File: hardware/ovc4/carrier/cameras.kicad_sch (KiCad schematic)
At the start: 7 parts, among them U1 Jetson_Nano, U12 PICAM, U13 PICAM, U14 PICAM, U15 PICAM, U16 PICAM, U17 PICAM

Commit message: Finished first iteration of placement and routing
Signed-off-by: Luca Della Vedova <luca@openrobotics.org>
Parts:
- added J7: Conn_01x05, Connector_PinHeader_2.54mm:PinHeader_1x05_P2.54mm_Vertical, symbol Connector_Generic:Conn_01x05
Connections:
- net CAM1_ENABLE: now also J7.3 (Pin_3)
- net CAM1_SCL_1V8: now also J7.4 (Pin_4)
- net CAM1_SDA_1V8: now also J7.5 (Pin_5)
- net CAM1_TRIGGER: now also J7.2 (Pin_2)
- net GND: now also J7.1 (Pin_1)
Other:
- note added: "For debugging"
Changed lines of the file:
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@@
   (junction (at 226.06 124.46))
   (junction (at 226.06 132.08))
+  (no_connect (at 39.37 128.27))
+  (no_connect (at 39.37 153.67))
+  (no_connect (at 39.37 138.43))
+  (no_connect (at 39.37 140.97))
+  (no_connect (at 39.37 125.73))
   (no_connect (at 39.37 130.81))
-  (no_connect (at 39.37 138.43))
+  (no_connect (at 39.37 156.21))
   (no_connect (at 39.37 133.35))
-  (no_connect (at 39.37 156.21))
   (no_connect (at 39.37 146.05))
-  (no_connect (at 39.37 153.67))
-  (no_connect (at 39.37 125.73))
-  (no_connect (at 39.37 128.27))
-  (no_connect (at 39.37 140.97))
   (no_connect (at 39.37 148.59))
   (wire (pts (xy 116.84 50.8) (xy 116.84 58.42)))
@@
   (wire (pts (xy 228.6 86.36) (xy 248.92 86.36)))
   (wire (pts (xy 228.6 144.78) (xy 248.92 144.78)))
+  (wire (pts (xy 231.14 27.94) (xy 251.46 27.94)))
   (text "TODO decide how to use only GPIO (or use ENABLE as gpio as well)"
     (at 200.66 25.4 0)
     (effects (font (size 1.27 1.27)) (justify right bottom))
   )
+  (text "For debugging" (at 256.54 25.4 180)
+    (effects (font (size 1.27 1.27)) (justify right bottom))
+  )
   (global_label "CAM0_CLK-" (shape input) (at 39.37 39.37 0)
     (effects (font (size 1.27 1.27)) (justify left))
@@
   )
   (global_label "CAM5_SDA_1V8" (shape input) (at 248.92 142.24 180)
+    (effects (font (size 1.27 1.27)) (justify right))
+  )
+  (global_label "CAM1_TRIGGER" (shape input) (at 251.46 30.48 180)
+    (effects (font (size 1.27 1.27)) (justify right))
+  )
+  (global_label "CAM1_ENABLE" (shape input) (at 251.46 33.02 180)
+    (effects (font (size 1.27 1.27)) (justify right))
+  )
+  (global_label "CAM1_SCL_1V8" (shape input) (at 251.46 35.56 180)
+    (effects (font (size 1.27 1.27)) (justify right))
+  )
+  (global_label "CAM1_SDA_1V8" (shape input) (at 251.46 38.1 180)
     (effects (font (size 1.27 1.27)) (justify right))
   )
@@
     )
   )
+  (symbol (lib_id "power:GND") (at 231.14 27.94 0) (unit 1)
+    (property "Reference" "#PWR0235" (id 0) (at 231.14 34.29 0)
+      (effects (font (size 1.27 1.27)) hide)
+    )
+    (property "Value" "GND" (id 1) (at 231.267 32.3342 0)
+      (effects (font (size 1.27 1.27)) hide)
+    )
+    (property "Footprint" "" (id 2) (at 231.14 27.94 0)
+      (effects (font (size 1.27 1.27)) hide)
+    )
+    (property "Datasheet" "" (id 3) (at 231.14 27.94 0)
+      (effects (font (size 1.27 1.27)) hide)
+    )
+  )
   (symbol (lib_id "power:GND") (at 259.08 91.44 0) (unit 1)
     (property "Reference" "#PWR0192" (id 0) (at 259.08 97.79 0)
@@
       (effects (font (size 1.27 1.27)) hide)
     )
+  )
+  (symbol (lib_id "Connector_Generic:Conn_01x05") (at 256.54 33.02 0) (unit 1)
+    (property "Reference" "J7" (id 0) (at 258.5721 31.9214 0)
+      (effects (font (size 1.27 1.27)) (justify left))
+    )
+    (property "Value" "Conn_01x05" (id 1) (at 258.5721 34.2201 0)
+      (effects (font (size 1.27 1.27)) (justify left))
+    )
+    (property "Footprint" "Connector_PinHeader_2.54mm:PinHeader_1x05_P2.54mm_Vertical" (id 2) (at 256.54 33.02 0)
+      (effects (font (size 1.27 1.27)) hide)
+    )
+    (property "Datasheet" "~" (id 3) (at 256.54 33.02 0)
+      (effects (font (size 1.27 1.27)) hide)
+    )

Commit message: Finished BOM and cosmetic changes
Signed-off-by: Luca Della Vedova <luca@openrobotics.org>
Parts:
- added TP6, TP7, TP8, TP9: Testpoint, TestPoint:TestPoint_Pad_D1.0mm, symbol Connector:TestPoint
- CAM0: renamed from U12; D1N (none) -> Digikey; D1PN (none) -> 609-1905-1-ND; MFN (none) -> Amphenol; MPN (none) -> SFW15R-1STE1LF
- CAM1: renamed from U14; D1N (none) -> Digikey; D1PN (none) -> 609-1905-1-ND; MFN (none) -> Amphenol; MPN (none) -> SFW15R-1STE1LF
- CAM2: renamed from U13; D1N (none) -> Digikey; D1PN (none) -> 609-1905-1-ND; MFN (none) -> Amphenol; MPN (none) -> SFW15R-1STE1LF
- CAM3: renamed from U15; D1N (none) -> Digikey; D1PN (none) -> 609-1905-1-ND; MFN (none) -> Amphenol; MPN (none) -> SFW15R-1STE1LF
- CAM4: renamed from U16; D1N (none) -> Digikey; D1PN (none) -> 609-1905-1-ND; MFN (none) -> Amphenol; MPN (none) -> SFW15R-1STE1LF
- CAM5: renamed from U17; D1N (none) -> Digikey; D1PN (none) -> 609-1905-1-ND; MFN (none) -> Amphenol; MPN (none) -> SFW15R-1STE1LF
- J7: value Conn_01x05 -> Conn_01x06; footprint Connector_PinHeader_2.54mm:PinHeader_1x05_P2.54mm_Vertical -> Connector_PinHeader_2.54mm:PinHeader_1x06_P2.54mm_Vertical; symbol Connector_Generic:Conn_01x05 -> Connector_Generic:Conn_01x06; D1N (none) -> Digikey; D1PN (none) -> 609-3263-ND; MFN (none) -> Amphenol; MPN (none) -> 68000-406HLF
- U1: D1N (none) -> Digikey; D1PN (none) -> A126764CT-ND; MFN (none) -> TE Connectivity; MPN (none) -> 2309413-1
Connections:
- net +3V3: now also J7.1 (Pin_1)
- net CAM0_ENABLE: now also TP9.1
- net CAM0_SCL_1V8: now also TP7.1
- net CAM0_SDA_1V8: now also TP6.1
- net CAM0_TRIGGER: now also TP8.1
- net CAM1_ENABLE: now also J7.4 (Pin_4); no longer J7.3 (Pin_3)
- net CAM1_SCL_1V8: now also J7.5 (Pin_5); no longer J7.4 (Pin_4)
- net CAM1_SDA_1V8: now also J7.6 (Pin_6); no longer J7.5 (Pin_5)
- net CAM1_TRIGGER: now also J7.3 (Pin_3); no longer J7.2 (Pin_2)
- net GND: now also J7.2 (Pin_2); no longer J7.1 (Pin_1)

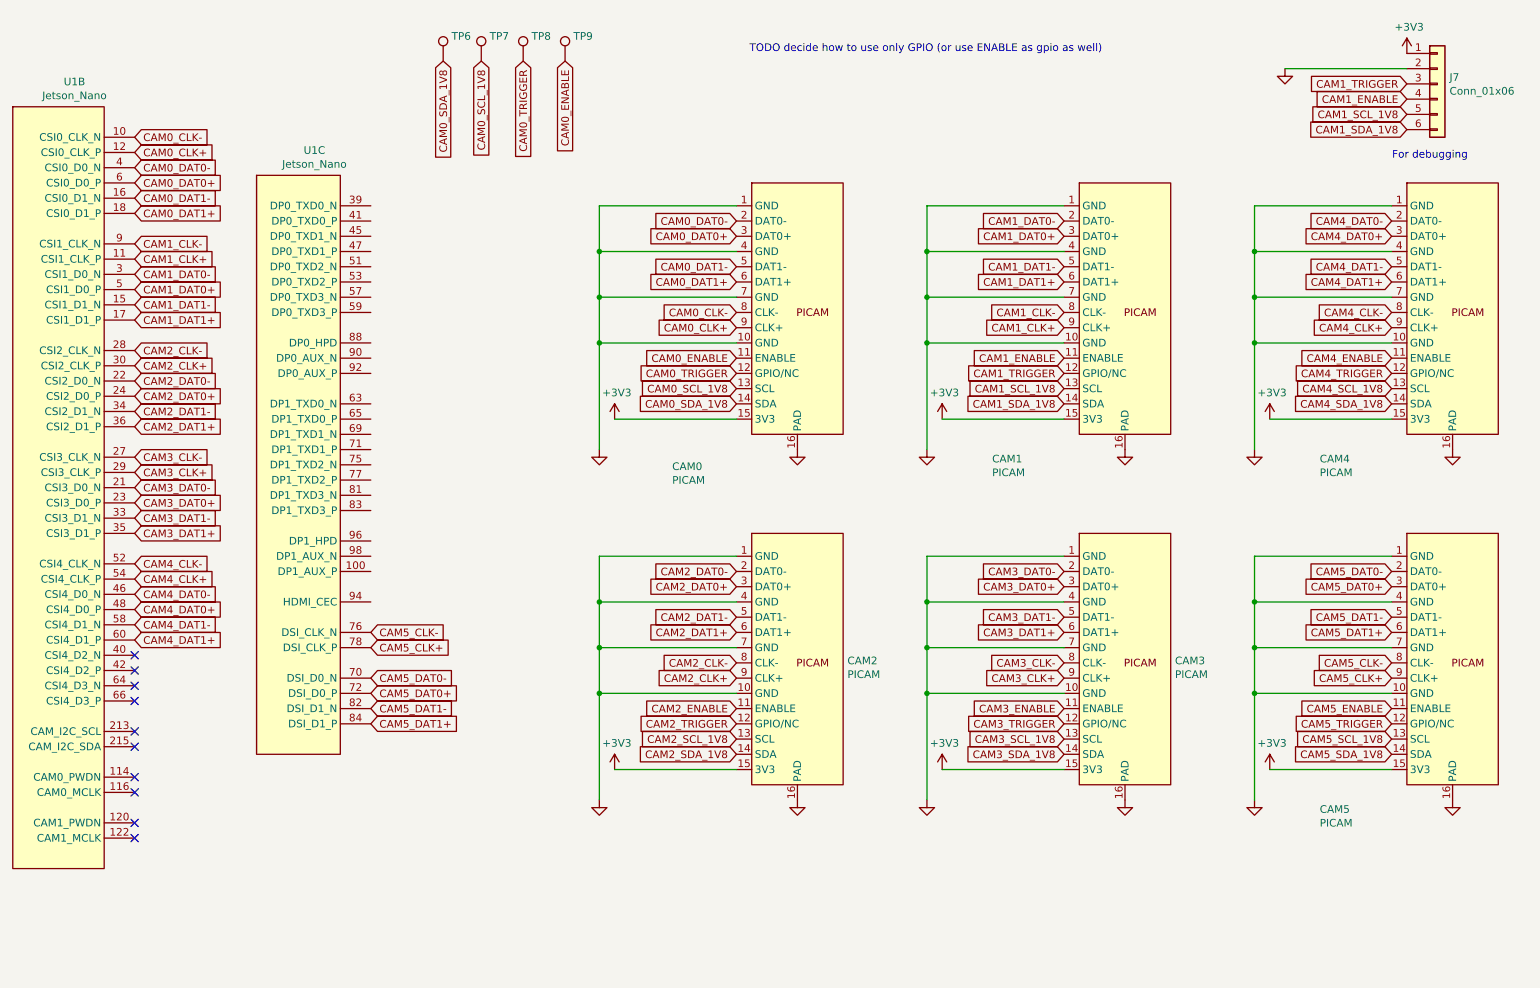
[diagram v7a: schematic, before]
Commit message: Added second fan header, added I2C pullups
Signed-off-by: Luca Della Vedova <luca@openrobotics.org>
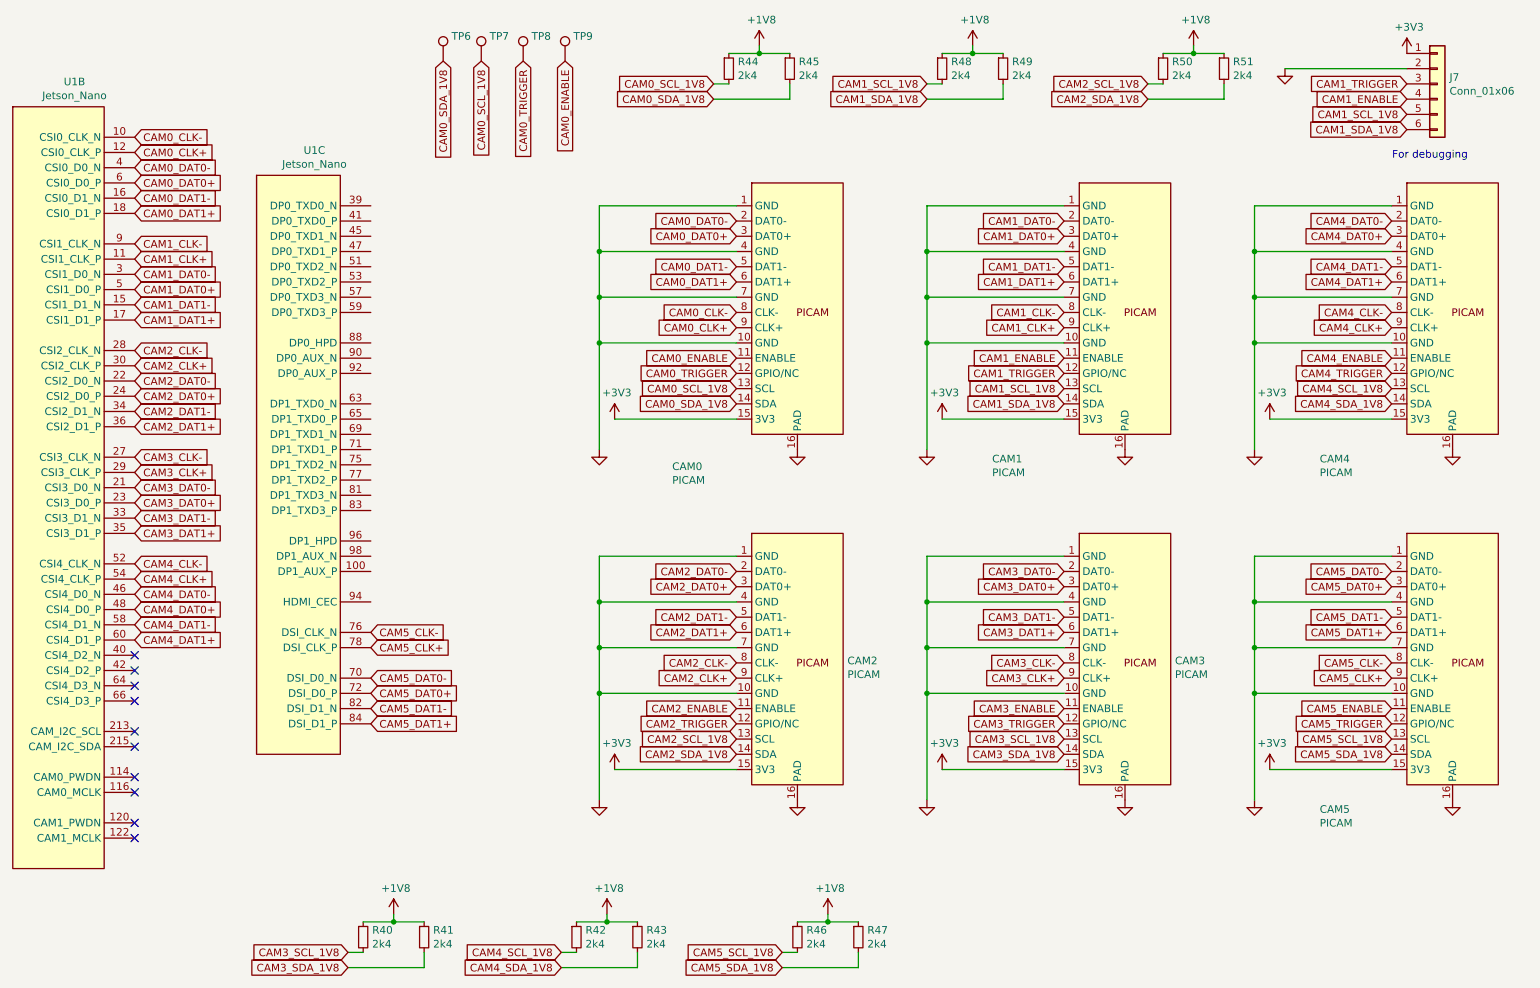
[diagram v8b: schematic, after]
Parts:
- added R40, R41, R42, R43, R44, R45, R46, R47, R48, R49, R50, R51: 2k4, Resistor_SMD:R_0402_1005Metric, symbol Device:R_Small
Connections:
- net CAM0_SCL_1V8: now also R44.2
- net CAM0_SDA_1V8: now also R45.2
- net CAM1_SCL_1V8: now also R48.2
- net CAM1_SDA_1V8: now also R49.2
- net CAM2_SCL_1V8: now also R50.2
- net CAM2_SDA_1V8: now also R51.2
- net CAM3_SCL_1V8: now also R40.2
- net CAM3_SDA_1V8: now also R41.2
- net CAM4_SCL_1V8: now also R42.2
- net CAM4_SDA_1V8: now also R43.2
- net CAM5_SCL_1V8: now also R46.2
- net CAM5_SDA_1V8: now also R47.2
- new net +1V8: R40.1, R41.1, R42.1, R43.1, R44.1, R45.1, R46.1, R47.1, R48.1, R49.1, R50.1, R51.1
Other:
- note removed: "TODO decide how to use only GPIO (or use ENABLE as gpio as well)"
